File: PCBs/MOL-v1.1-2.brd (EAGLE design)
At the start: 165.1 x 81 mm, 60 parts, among them IC1 ULN2803, IC2 ULN2803, IC3 SN74LVC2G04DBV, J1 SERVO 1, J2 SERVO 2, J3 SERVO 3

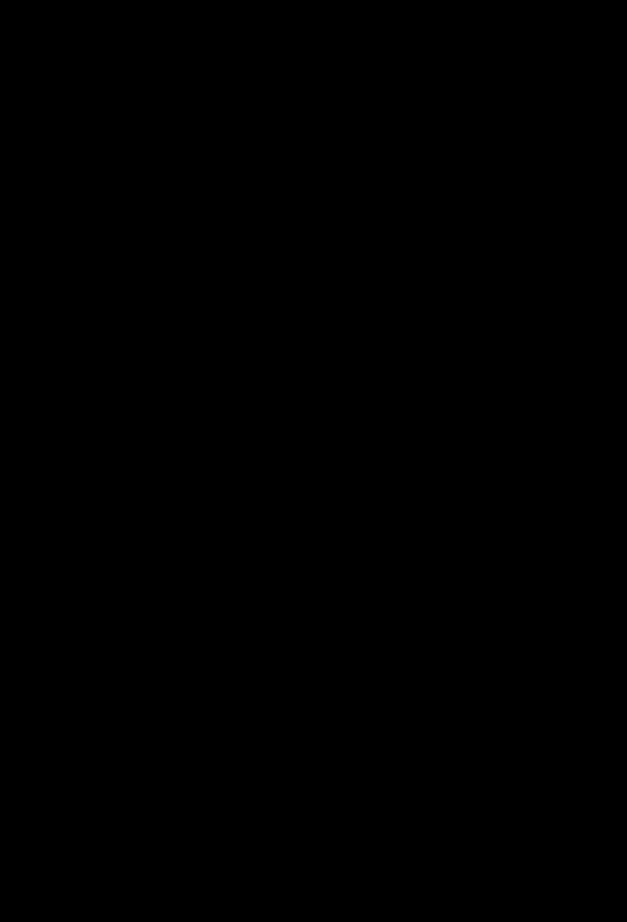
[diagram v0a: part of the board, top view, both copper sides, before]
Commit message: version v2-1 of MOL board, ACTUATOR and STRIP modules
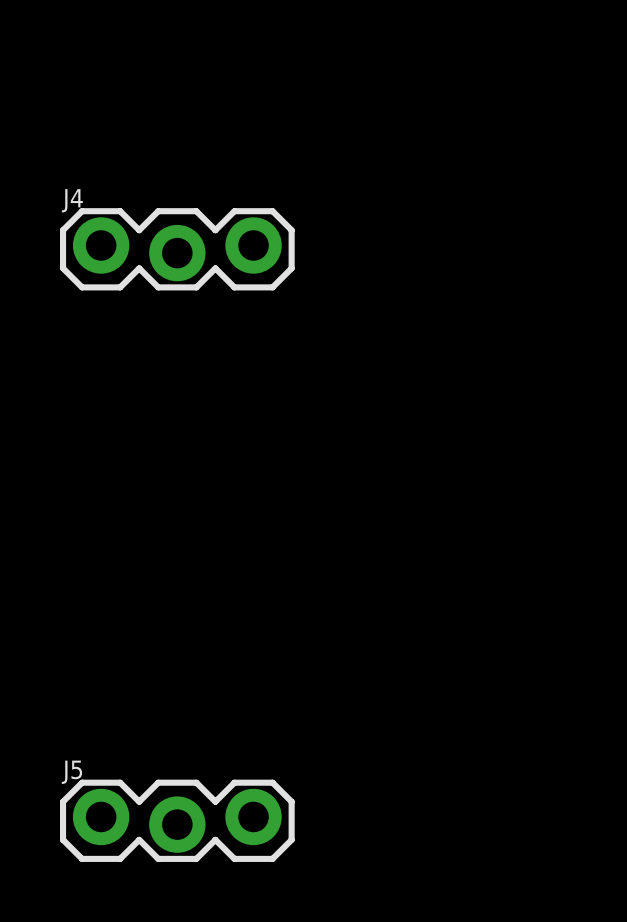
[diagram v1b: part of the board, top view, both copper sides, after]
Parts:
- added J4: SERVO 1, SparkFun-Connectors:1X03_LOCK@1
- added J5: SERVO 2, SparkFun-Connectors:1X03_LOCK@1
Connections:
- net +5V: now also J4.2, J5.2
- net GND: now also J4.1, J5.1
- net S1: now also J4.3
- net S2: now also J5.3
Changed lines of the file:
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@@
 </element>
 <element name="AN-IN-12" library="SparkFun-Connectors" package="1X03_NO_SILK" value="" x="214.376" y="77.343"/>
+<element name="J4" library="SparkFun-Connectors" package="1X03_LOCK@1" value="SERVO 1" x="-1.27" y="-26.67"/>
+<element name="J5" library="SparkFun-Connectors" package="1X03_LOCK@1" value="SERVO 2" x="-1.27" y="-45.72"/>
 </elements>
 <signals>
@@
 <contactref element="S11" pad="3"/>
 <contactref element="S12" pad="3"/>
+<contactref element="J4" pad="1"/>
+<contactref element="J5" pad="1"/>
 <wire x1="191.77" y1="43.18" x2="203.2" y2="43.18" width="0" layer="19" extent="1-1"/>
 <wire x1="214.63" y1="43.18" x2="203.2" y2="43.18" width="0" layer="19" extent="1-1"/>
@@
 <wire x1="59.69" y1="12.7" x2="46.99" y2="12.7" width="0" layer="19" extent="1-1"/>
 <wire x1="91.44" y1="5.08" x2="91.44" y2="36.83" width="0" layer="19" extent="1-1"/>
+<wire x1="-1.27" y1="-26.543" x2="16.51" y2="12.7" width="0" layer="19" extent="1-1"/>
+<wire x1="-1.27" y1="-45.593" x2="-1.27" y2="-26.543" width="0" layer="19" extent="1-1"/>
 </signal>
 <signal name="B1">
@@
 <contactref element="VIN" pad="1"/>
 <contactref element="J3" pad="2"/>
+<contactref element="J4" pad="2"/>
+<contactref element="J5" pad="2"/>
 <wire x1="158.242" y1="24.13" x2="162.687" y2="24.13" width="0" layer="19" extent="1-1"/>
 <wire x1="153.797" y1="24.13" x2="158.242" y2="24.13" width="0" layer="19" extent="1-1"/>
@@
 <wire x1="91.44" y1="12.7" x2="154.04" y2="7.62" width="0" layer="19" extent="1-1"/>
 <wire x1="6.35" y1="31.75" x2="91.44" y2="12.7" width="0" layer="19" extent="1-1"/>
+<wire x1="1.27" y1="-26.797" x2="6.35" y2="31.75" width="0" layer="19" extent="1-1"/>
+<wire x1="1.27" y1="-45.847" x2="1.27" y2="-26.797" width="0" layer="19" extent="1-1"/>
 </signal>
 <signal name="S1">
 <contactref element="J1" pad="3"/>
 <contactref element="TEENSY" pad="9"/>
+<contactref element="J4" pad="3"/>
 <wire x1="26.67" y1="20.32" x2="153.543" y2="26.67" width="0" layer="19" extent="1-1"/>
+<wire x1="3.81" y1="-26.543" x2="26.67" y2="20.32" width="0" layer="19" extent="1-1"/>
 </signal>
 <signal name="S2">
 <contactref element="TEENSY" pad="10"/>
 <contactref element="J2" pad="3"/>
+<contactref element="J5" pad="3"/>
 <wire x1="29.21" y1="20.32" x2="157.988" y2="26.67" width="0" layer="19" extent="1-1"/>
+<wire x1="3.81" y1="-45.593" x2="29.21" y2="20.32" width="0" layer="19" extent="1-1"/>
 </signal>
 <signal name="L2">
